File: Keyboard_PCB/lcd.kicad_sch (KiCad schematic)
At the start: 11 parts, among them Q2 S8050

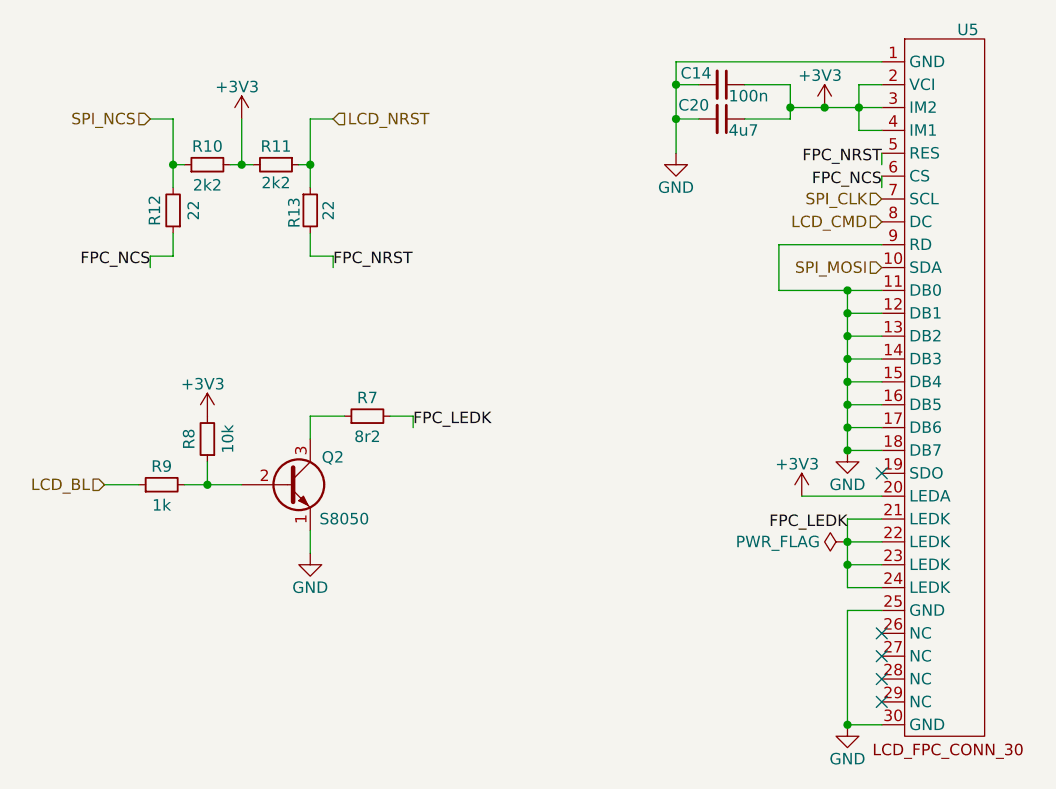
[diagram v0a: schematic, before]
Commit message: Fixed errors in BOM file
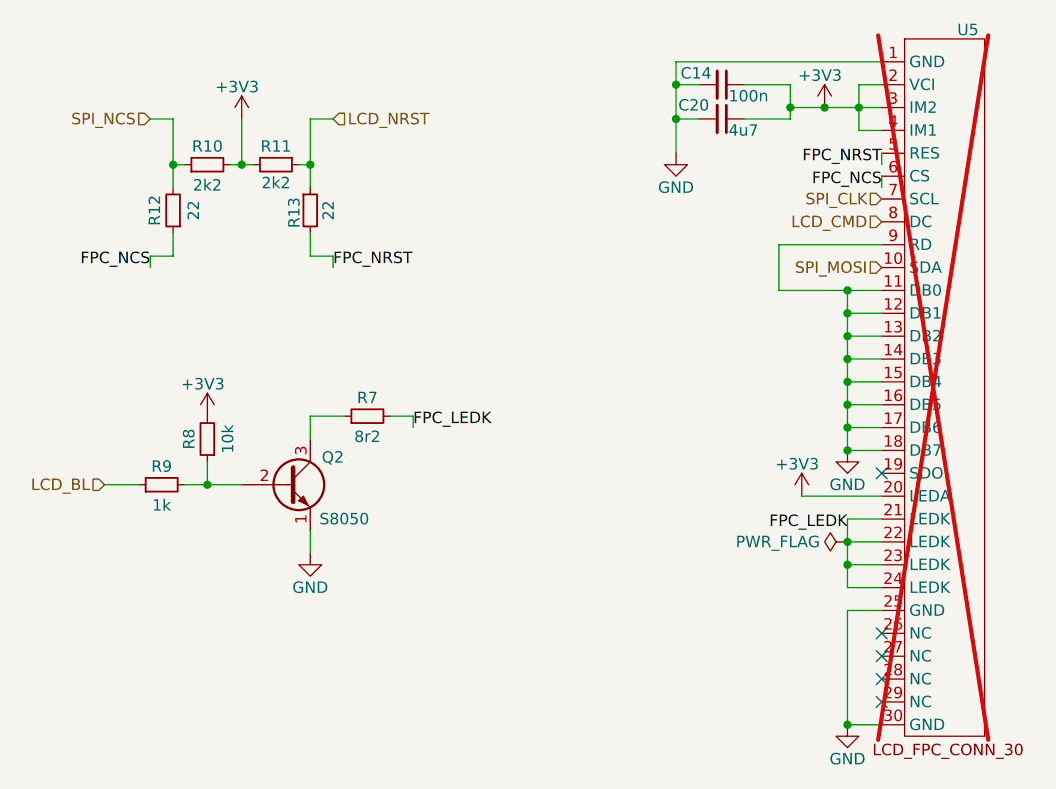
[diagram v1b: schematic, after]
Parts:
- U5: now not fitted
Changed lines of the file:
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@@
 		(in_bom yes)
 		(on_board yes)
-		(dnp no)
+		(dnp yes)
 		(property "Reference" "U5"
 			(at 217.932 39.624 0)

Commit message: Finished Layout V1
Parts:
- C14: footprint Capacitor_SMD:C_0402_1005Metric -> Capacitor_SMD:C_0603_1608Metric
- C20: footprint Capacitor_SMD:C_0402_1005Metric -> Capacitor_SMD:C_0603_1608Metric; LCSC C23733 -> (none)
- R10, R11, R12, R13, R7, R8, R9: footprint Resistor_SMD:R_0402_1005Metric -> Resistor_SMD:R_0603_1608Metric
- U5: now fitted
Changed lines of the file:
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@@
 			)
 		)
-		(property "Footprint" "Capacitor_SMD:C_0402_1005Metric"
+		(property "Footprint" "Capacitor_SMD:C_0603_1608Metric"
 			(at 191.77 49.53 0)
 			(effects
@@
 			)
 		)
-		(property "LCSC" "C23733"
+		(property "LCSC" ""
 			(at 191.77 49.53 0)
 			(effects
@@
 			)
 		)
-		(property "Footprint" "Resistor_SMD:R_0402_1005Metric"
+		(property "Footprint" "Resistor_SMD:R_0603_1608Metric"
 			(at 129.54 90.17 0)
 			(effects
@@
 			)
 		)
-		(property "Footprint" "Resistor_SMD:R_0402_1005Metric"
+		(property "Footprint" "Resistor_SMD:R_0603_1608Metric"
 			(at 134.62 54.61 0)
 			(effects
@@
 			)
 		)
-		(property "Footprint" "Resistor_SMD:R_0402_1005Metric"
+		(property "Footprint" "Resistor_SMD:R_0603_1608Metric"
 			(at 152.4 82.55 0)
 			(effects
@@
 		(in_bom yes)
 		(on_board yes)
-		(dnp yes)
+		(dnp no)
 		(property "Reference" "U5"
 			(at 217.932 39.624 0)
@@
 			)
 		)
-		(property "Footprint" "Resistor_SMD:R_0402_1005Metric"
+		(property "Footprint" "Resistor_SMD:R_0603_1608Metric"
 			(at 142.24 54.61 0)
 			(effects
@@
 			)
 		)
-		(property "Footprint" "Resistor_SMD:R_0402_1005Metric"
+		(property "Footprint" "Resistor_SMD:R_0603_1608Metric"
 			(at 146.05 59.69 0)
 			(effects
@@
 			)
 		)
-		(property "Footprint" "Capacitor_SMD:C_0402_1005Metric"
+		(property "Footprint" "Capacitor_SMD:C_0603_1608Metric"
 			(at 191.77 45.72 0)
 			(effects
@@
 			)
 		)
-		(property "Footprint" "Resistor_SMD:R_0402_1005Metric"
+		(property "Footprint" "Resistor_SMD:R_0603_1608Metric"
 			(at 134.62 85.09 0)
 			(effects
@@
 			)
 		)
-		(property "Footprint" "Resistor_SMD:R_0402_1005Metric"
+		(property "Footprint" "Resistor_SMD:R_0603_1608Metric"
 			(at 130.81 59.69 0)
 			(effects
